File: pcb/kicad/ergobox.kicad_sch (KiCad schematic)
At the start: 72 parts, among them SW1 SW_Push, SW10 Kailh, SW11 Kailh, SW12 Kailh, SW13 Kailh, SW14 Kailh, SW15 Kailh, SW16 Kailh, SW17 Kailh, SW18 Kailh, SW19 Kailh, SW2 SW_Push, SW20 Kailh, SW3 SW_Push, SW4 SW_Push, SW5 SW_Push, SW6 SW_Push, SW7 SW_Push, SW8 SW_Push, SW9 Kailh, U1 TLV73333PDBV, U2 RP2040, U3 W25Q128JVS, Y1 Crystal_GND24

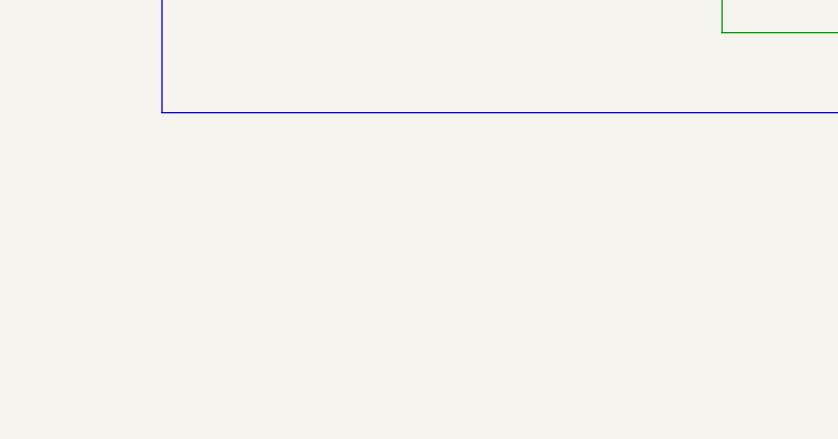
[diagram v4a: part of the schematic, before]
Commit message: feat: adds M4 mounting holes to schematic
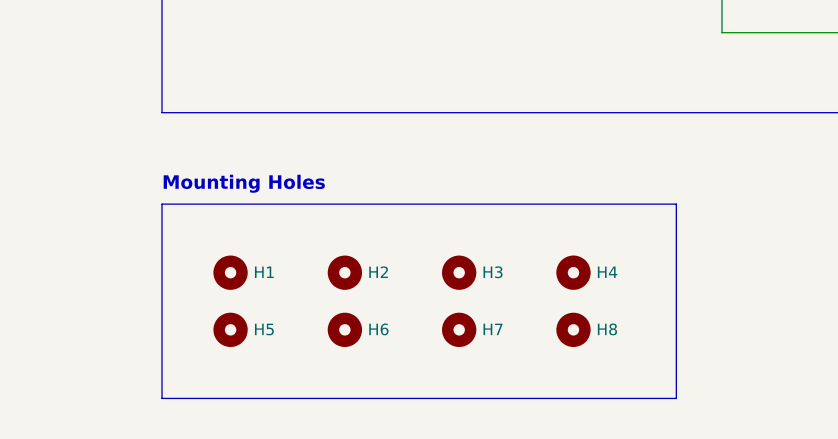
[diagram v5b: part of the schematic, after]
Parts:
- added H1, H2, H3, H4, H5, H6, H7, H8: MountingHole, MountingHole:MountingHole_4.3mm_M4, symbol Mechanical:MountingHole
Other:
- note added: "Mounting Holes"
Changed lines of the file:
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@@
     (stroke (width 0) (type default) (color 0 0 0 0))
   )
+  (polyline (pts (xy 260.35 280.67) (xy 203.2 280.67))
+    (stroke (width 0) (type default) (color 0 0 0 0))
+  )
   (wire (pts (xy 36.83 81.28) (xy 53.34 81.28))
     (stroke (width 0) (type default) (color 0 0 0 0))
@@
     (stroke (width 0) (type default) (color 0 0 0 0))
   )
+  (polyline (pts (xy 203.2 259.08) (xy 260.35 259.08))
+    (stroke (width 0) (type default) (color 0 0 0 0))
+  )
   (wire (pts (xy 111.76 40.64) (xy 111.76 44.45))
     (stroke (width 0) (type default) (color 0 0 0 0))
@@
     (stroke (width 0) (type default) (color 0 0 0 0))
   )
+  (polyline (pts (xy 203.2 259.08) (xy 203.2 280.67))
+    (stroke (width 0) (type default) (color 0 0 0 0))
+  )
   (wire (pts (xy 64.77 46.99) (xy 64.77 55.88))
     (stroke (width 0) (type default) (color 0 0 0 0))
@@
     (stroke (width 0) (type default) (color 0 0 0 0))
   )
+  (polyline (pts (xy 260.35 259.08) (xy 260.35 280.67))
+    (stroke (width 0) (type default) (color 0 0 0 0))
+  )
   (wire (pts (xy 44.45 204.47) (xy 71.12 204.47))
     (stroke (width 0) (type default) (color 0 0 0 0))
@@
     (effects (font (size 1.5 1.5) bold) (justify left bottom))
   )
+  (text "Mounting Holes\n" (at 203.2 257.81 0)
+    (effects (font (size 1.5 1.5) bold) (justify left bottom))
+  )
   (text "Switches" (at 203.2 19.05 0)
     (effects (font (size 1.5 1.5) bold) (justify left bottom))
@@
     (pin "2")
   )
+  (symbol (lib_id "Mechanical:MountingHole") (at 236.22 273.05 0) (unit 1)
+    (in_bom yes) (on_board yes) (fields_autoplaced)
+    (property "Reference" "H7" (id 0) (at 238.76 273.0499 0)
+      (effects (font (size 1.27 1.27)) (justify left))
+    )
+    (property "Value" "MountingHole" (id 1) (at 238.76 274.3199 0)
+      (effects (font (size 1.27 1.27)) (justify left) hide)
+    )
+    (property "Footprint" "MountingHole:MountingHole_4.3mm_M4" (id 2) (at 236.22 273.05 0)
+      (effects (font (size 1.27 1.27)) hide)
+    )
+    (property "Datasheet" "~" (id 3) (at 236.22 273.05 0)
+      (effects (font (size 1.27 1.27)) hide)
+    )
+  )
   (symbol (lib_id "Switch:SW_Push") (at 43.18 127 0) (unit 1)
     (in_bom yes) (on_board yes) (fields_autoplaced)
@@
     (pin "1")
   )
+  (symbol (lib_id "Mechanical:MountingHole") (at 248.92 273.05 0) (unit 1)
+    (in_bom yes) (on_board yes) (fields_autoplaced)
+    (property "Reference" "H8" (id 0) (at 251.46 273.0499 0)
+      (effects (font (size 1.27 1.27)) (justify left))
+    )
+    (property "Value" "MountingHole" (id 1) (at 251.46 274.3199 0)
+      (effects (font (size 1.27 1.27)) (justify left) hide)
+    )
+    (property "Footprint" "MountingHole:MountingHole_4.3mm_M4" (id 2) (at 248.92 273.05 0)
+      (effects (font (size 1.27 1.27)) hide)
+    )
+    (property "Datasheet" "~" (id 3) (at 248.92 273.05 0)
+      (effects (font (size 1.27 1.27)) hide)
+    )
+  )
   (symbol (lib_id "Device:C") (at 69.85 264.16 0) (unit 1)
     (in_bom yes) (on_board yes) (fields_autoplaced)
@@
     (pin "2")
   )
+  (symbol (lib_id "Mechanical:MountingHole") (at 223.52 273.05 0) (unit 1)
+    (in_bom yes) (on_board yes) (fields_autoplaced)
+    (property "Reference" "H6" (id 0) (at 226.06 273.0499 0)
+      (effects (font (size 1.27 1.27)) (justify left))
+    )
+    (property "Value" "MountingHole" (id 1) (at 226.06 274.3199 0)
+      (effects (font (size 1.27 1.27)) (justify left) hide)
+    )
+    (property "Footprint" "MountingHole:MountingHole_4.3mm_M4" (id 2) (at 223.52 273.05 0)
+      (effects (font (size 1.27 1.27)) hide)
+    )
+    (property "Datasheet" "~" (id 3) (at 223.52 273.05 0)
+      (effects (font (size 1.27 1.27)) hide)
+    )
+  )
   (symbol (lib_id "USB-C:HRO-TYPE-C-31-M-12") (at 41.91 205.74 0) (unit 1)
     (in_bom yes) (on_board yes)
@@
     (pin "2")
   )
+  (symbol (lib_id "Mechanical:MountingHole") (at 210.82 266.7 0) (unit 1)
+    (in_bom yes) (on_board yes) (fields_autoplaced)
+    (property "Reference" "H1" (id 0) (at 213.36 266.6999 0)
+      (effects (font (size 1.27 1.27)) (justify left))
+    )
+    (property "Value" "MountingHole" (id 1) (at 213.36 267.9699 0)
+      (effects (font (size 1.27 1.27)) (justify left) hide)
+    )
+    (property "Footprint" "MountingHole:MountingHole_4.3mm_M4" (id 2) (at 210.82 266.7 0)
+      (effects (font (size 1.27 1.27)) hide)
+    )
+    (property "Datasheet" "~" (id 3) (at 210.82 266.7 0)
+      (effects (font (size 1.27 1.27)) hide)
+    )
+  )
   (symbol (lib_id "power:GND") (at 69.85 270.51 0) (unit 1)
     (in_bom yes) (on_board yes) (fields_autoplaced)
@@
     (pin "1")
   )
+  (symbol (lib_id "Mechanical:MountingHole") (at 223.52 266.7 0) (unit 1)
+    (in_bom yes) (on_board yes) (fields_autoplaced)
+    (property "Reference" "H2" (id 0) (at 226.06 266.6999 0)
+      (effects (font (size 1.27 1.27)) (justify left))
+    )
+    (property "Value" "MountingHole" (id 1) (at 226.06 267.9699 0)
+      (effects (font (size 1.27 1.27)) (justify left) hide)
+    )
+    (property "Footprint" "MountingHole:MountingHole_4.3mm_M4" (id 2) (at 223.52 266.7 0)
+      (effects (font (size 1.27 1.27)) hide)
+    )
+    (property "Datasheet" "~" (id 3) (at 223.52 266.7 0)
+      (effects (font (size 1.27 1.27)) hide)
+    )
+  )
   (symbol (lib_id "Switch:SW_Push") (at 266.7 46.99 0) (unit 1)
     (in_bom yes) (on_board yes) (fields_autoplaced)
@@
     (pin "4")
   )
+  (symbol (lib_id "Mechanical:MountingHole") (at 210.82 273.05 0) (unit 1)
+    (in_bom yes) (on_board yes) (fields_autoplaced)
+    (property "Reference" "H5" (id 0) (at 213.36 273.0499 0)
+      (effects (font (size 1.27 1.27)) (justify left))
+    )
+    (property "Value" "MountingHole" (id 1) (at 213.36 274.3199 0)
+      (effects (font (size 1.27 1.27)) (justify left) hide)
+    )
+    (property "Footprint" "MountingHole:MountingHole_4.3mm_M4" (id 2) (at 210.82 273.05 0)
+      (effects (font (size 1.27 1.27)) hide)
+    )
+    (property "Datasheet" "~" (id 3) (at 210.82 273.05 0)
+      (effects (font (size 1.27 1.27)) hide)
+    )
+  )
   (symbol (lib_id "Device:C") (at 256.54 195.58 0) (unit 1)
     (in_bom yes) (on_board yes)
@@
     (pin "1")
   )
+  (symbol (lib_id "Mechanical:MountingHole") (at 236.22 266.7 0) (unit 1)
+    (in_bom yes) (on_board yes) (fields_autoplaced)
+    (property "Reference" "H3" (id 0) (at 238.76 266.6999 0)
+      (effects (font (size 1.27 1.27)) (justify left))
+    )
+    (property "Value" "MountingHole" (id 1) (at 238.76 267.9699 0)
+      (effects (font (size 1.27 1.27)) (justify left) hide)
+    )
+    (property "Footprint" "MountingHole:MountingHole_4.3mm_M4" (id 2) (at 236.22 266.7 0)
+      (effects (font (size 1.27 1.27)) hide)
+    )
+    (property "Datasheet" "~" (id 3) (at 236.22 266.7 0)
+      (effects (font (size 1.27 1.27)) hide)
+    )
+  )
   (symbol (lib_id "Device:C") (at 167.64 36.83 0) (unit 1)
     (in_bom yes) (on_board yes) (fields_autoplaced)
@@
     (pin "2")
   )
+  (symbol (lib_id "Mechanical:MountingHole") (at 248.92 266.7 0) (unit 1)
+    (in_bom yes) (on_board yes) (fields_autoplaced)
+    (property "Reference" "H4" (id 0) (at 251.46 266.6999 0)
+      (effects (font (size 1.27 1.27)) (justify left))
+    )
+    (property "Value" "MountingHole" (id 1) (at 251.46 267.9699 0)
+      (effects (font (size 1.27 1.27)) (justify left) hide)
+    )
+    (property "Footprint" "MountingHole:MountingHole_4.3mm_M4" (id 2) (at 248.92 266.7 0)
+      (effects (font (size 1.27 1.27)) hide)
+    )
+    (property "Datasheet" "~" (id 3) (at 248.92 266.7 0)
+      (effects (font (size 1.27 1.27)) hide)
+    )
+  )
   (symbol (lib_id "Switch:SW_Push") (at 110.49 269.24 90) (unit 1)
     (in_bom yes) (on_board yes)
@@
       (reference "D12") (unit 1) (value "WS2812C-2020") (footprint "WS2812C-2020:LED_WS2812C-2020")
     )
+    (path "/687e50ab-3031-4d58-8b19-d1b9b19cede1"
+      (reference "H1") (unit 1) (value "MountingHole") (footprint "MountingHole:MountingHole_4.3mm_M4")
+    )
+    (path "/6c8cfcb3-2d0d-4436-a20a-c00cae63ff2f"
+      (reference "H2") (unit 1) (value "MountingHole") (footprint "MountingHole:MountingHole_4.3mm_M4")
+    )
+    (path "/8a16ad91-6558-4e06-9814-73d3ba261d92"
+      (reference "H3") (unit 1) (value "MountingHole") (footprint "MountingHole:MountingHole_4.3mm_M4")
+    )
+    (path "/da7f181c-d15d-4405-8b7c-eeb7f5b635a9"
+      (reference "H4") (unit 1) (value "MountingHole") (footprint "MountingHole:MountingHole_4.3mm_M4")
+    )
+    (path "/80f2d6a0-2d04-463b-980a-3c1edca108b9"
+      (reference "H5") (unit 1) (value "MountingHole") (footprint "MountingHole:MountingHole_4.3mm_M4")
+    )
+    (path "/3f875e20-671c-43b5-8a63-545e16b7fd63"
+      (reference "H6") (unit 1) (value "MountingHole") (footprint "MountingHole:MountingHole_4.3mm_M4")
+    )
+    (path "/2bc49a6e-0559-4615-be88-bf9131f58e2b"
+      (reference "H7") (unit 1) (value "MountingHole") (footprint "MountingHole:MountingHole_4.3mm_M4")
+    )
+    (path "/3435fb98-ae2e-4861-b6f5-7fd7a7ca1bfc"
+      (reference "H8") (unit 1) (value "MountingHole") (footprint "MountingHole:MountingHole_4.3mm_M4")
+    )
     (path "/f641fac0-9443-4e6d-9146-0822ee3cea7e"

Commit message: feat: initial PCB setup
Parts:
- H5: footprint MountingHole:MountingHole_4.3mm_M4 -> MountingHole:MountingHole_3.2mm_M3
- U2: footprint RP2040_minimal:RP2040-QFN-56 -> RP2040:RP2040-QFN-56
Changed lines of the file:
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@@
       (effects (font (size 1.27 1.27)) (justify left) hide)
     )
-    (property "Footprint" "MountingHole:MountingHole_4.3mm_M4" (id 2) (at 210.82 273.05 0)
+    (property "Footprint" "MountingHole:MountingHole_3.2mm_M3" (id 2) (at 210.82 273.05 0)
       (effects (font (size 1.27 1.27)) hide)
     )
@@
       (effects (font (size 1.27 1.27)) (justify left))
     )
-    (property "Footprint" "RP2040_minimal:RP2040-QFN-56" (id 2) (at 66.04 106.68 0)
+    (property "Footprint" "RP2040:RP2040-QFN-56" (id 2) (at 66.04 106.68 0)
       (effects (font (size 1.27 1.27)) hide)
     )
@@
     )
     (path "/80f2d6a0-2d04-463b-980a-3c1edca108b9"
-      (reference "H5") (unit 1) (value "MountingHole") (footprint "MountingHole:MountingHole_4.3mm_M4")
+      (reference "H5") (unit 1) (value "MountingHole") (footprint "MountingHole:MountingHole_3.2mm_M3")
     )
     (path "/3f875e20-671c-43b5-8a63-545e16b7fd63"
@@
     )
     (path "/9ba26deb-2dd5-446d-bf34-3cafd3f511c3"
-      (reference "U2") (unit 1) (value "RP2040") (footprint "RP2040_minimal:RP2040-QFN-56")
+      (reference "U2") (unit 1) (value "RP2040") (footprint "RP2040:RP2040-QFN-56")
     )
     (path "/91d5d34b-e030-491a-8afc-6eb190fc6b2f"

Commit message: refactor: changes kailh footprints to hotswap non-optionals.
The kailh low footprints with optional hotswaps are not symmetric.
In the optional footprint, the hotswap switch pad goes through the RGB footpad,
so it cannot be used.
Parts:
- SW10, SW11, SW12, SW13, SW14, SW15, SW16, SW17, SW18, SW19, SW20, SW9: footprint Keyswitches:Kailh_socket_PG1350_optional -> Keyswitches:Kailh_socket_PG1350
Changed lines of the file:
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@@
     (property "Reference" "SW11" (id 0) (at 266.7 50.8 0))
     (property "Value" "Kailh" (id 1) (at 266.7 53.34 0))
-    (property "Footprint" "Keyswitches:Kailh_socket_PG1350_optional" (id 2) (at 266.7 53.34 0)
+    (property "Footprint" "Keyswitches:Kailh_socket_PG1350" (id 2) (at 266.7 53.34 0)
       (effects (font (size 1.27 1.27)) hide)
     )
@@
     (property "Reference" "SW17" (id 0) (at 344.17 27.94 0))
     (property "Value" "Kailh" (id 1) (at 344.17 30.48 0))
-    (property "Footprint" "Keyswitches:Kailh_socket_PG1350_optional" (id 2) (at 344.17 30.48 0)
+    (property "Footprint" "Keyswitches:Kailh_socket_PG1350" (id 2) (at 344.17 30.48 0)
       (effects (font (size 1.27 1.27)) hide)
     )
@@
     (property "Reference" "SW16" (id 0) (at 304.8 62.23 0))
     (property "Value" "Kailh" (id 1) (at 304.8 64.77 0))
-    (property "Footprint" "Keyswitches:Kailh_socket_PG1350_optional" (id 2) (at 304.8 64.77 0)
+    (property "Footprint" "Keyswitches:Kailh_socket_PG1350" (id 2) (at 304.8 64.77 0)
       (effects (font (size 1.27 1.27)) hide)
     )
@@
     (property "Reference" "SW12" (id 0) (at 266.7 62.23 0))
     (property "Value" "Kailh" (id 1) (at 266.7 64.77 0))
-    (property "Footprint" "Keyswitches:Kailh_socket_PG1350_optional" (id 2) (at 266.7 64.77 0)
+    (property "Footprint" "Keyswitches:Kailh_socket_PG1350" (id 2) (at 266.7 64.77 0)
       (effects (font (size 1.27 1.27)) hide)
     )
@@
     (property "Reference" "SW14" (id 0) (at 304.8 39.37 0))
     (property "Value" "Kailh" (id 1) (at 304.8 41.91 0))
-    (property "Footprint" "Keyswitches:Kailh_socket_PG1350_optional" (id 2) (at 304.8 41.91 0)
+    (property "Footprint" "Keyswitches:Kailh_socket_PG1350" (id 2) (at 304.8 41.91 0)
       (effects (font (size 1.27 1.27)) hide)
     )
@@
     (property "Reference" "SW20" (id 0) (at 344.17 62.23 0))
     (property "Value" "Kailh" (id 1) (at 344.17 64.77 0))
-    (property "Footprint" "Keyswitches:Kailh_socket_PG1350_optional" (id 2) (at 344.17 64.77 0)
+    (property "Footprint" "Keyswitches:Kailh_socket_PG1350" (id 2) (at 344.17 64.77 0)
       (effects (font (size 1.27 1.27)) hide)
     )
@@
     (property "Reference" "SW10" (id 0) (at 266.7 39.37 0))
     (property "Value" "Kailh" (id 1) (at 266.7 41.91 0))
-    (property "Footprint" "Keyswitches:Kailh_socket_PG1350_optional" (id 2) (at 266.7 41.91 0)
+    (property "Footprint" "Keyswitches:Kailh_socket_PG1350" (id 2) (at 266.7 41.91 0)
       (effects (font (size 1.27 1.27)) hide)
     )
@@
     (property "Reference" "SW19" (id 0) (at 344.17 50.8 0))
     (property "Value" "Kailh" (id 1) (at 344.17 53.34 0))
-    (property "Footprint" "Keyswitches:Kailh_socket_PG1350_optional" (id 2) (at 344.17 53.34 0)
+    (property "Footprint" "Keyswitches:Kailh_socket_PG1350" (id 2) (at 344.17 53.34 0)
       (effects (font (size 1.27 1.27)) hide)
     )
@@
     (property "Reference" "SW18" (id 0) (at 344.17 39.37 0))
     (property "Value" "Kailh" (id 1) (at 344.17 41.91 0))
-    (property "Footprint" "Keyswitches:Kailh_socket_PG1350_optional" (id 2) (at 344.17 41.91 0)
+    (property "Footprint" "Keyswitches:Kailh_socket_PG1350" (id 2) (at 344.17 41.91 0)
       (effects (font (size 1.27 1.27)) hide)
     )
@@
     (property "Reference" "SW15" (id 0) (at 304.8 50.8 0))
     (property "Value" "Kailh" (id 1) (at 304.8 53.34 0))
-    (property "Footprint" "Keyswitches:Kailh_socket_PG1350_optional" (id 2) (at 304.8 53.34 0)
+    (property "Footprint" "Keyswitches:Kailh_socket_PG1350" (id 2) (at 304.8 53.34 0)
       (effects (font (size 1.27 1.27)) hide)
     )
@@
     (property "Reference" "SW9" (id 0) (at 266.7 27.94 0))
     (property "Value" "Kailh" (id 1) (at 266.7 30.48 0))
-    (property "Footprint" "Keyswitches:Kailh_socket_PG1350_optional" (id 2) (at 266.7 30.48 0)
+    (property "Footprint" "Keyswitches:Kailh_socket_PG1350" (id 2) (at 266.7 30.48 0)
       (effects (font (size 1.27 1.27)) hide)
     )
@@
     (property "Reference" "SW13" (id 0) (at 304.8 27.94 0))
     (property "Value" "Kailh" (id 1) (at 304.8 30.48 0))
-    (property "Footprint" "Keyswitches:Kailh_socket_PG1350_optional" (id 2) (at 304.8 30.48 0)
+    (property "Footprint" "Keyswitches:Kailh_socket_PG1350" (id 2) (at 304.8 30.48 0)
       (effects (font (size 1.27 1.27)) hide)
     )
@@
     )
     (path "/e7e50001-1420-4b1c-9a9c-244be6cee891"
-      (reference "SW9") (unit 1) (value "Kailh") (footprint "Keyswitches:Kailh_socket_PG1350_optional")
+      (reference "SW9") (unit 1) (value "Kailh") (footprint "Keyswitches:Kailh_socket_PG1350")
     )
     (path "/6ffa2bda-adb8-4b45-b2f3-66d14af70739"
-      (reference "SW10") (unit 1) (value "Kailh") (footprint "Keyswitches:Kailh_socket_PG1350_optional")
+      (reference "SW10") (unit 1) (value "Kailh") (footprint "Keyswitches:Kailh_socket_PG1350")
     )
     (path "/0d5161b8-5c58-4924-99b4-8ca9b7edfc0a"
-      (reference "SW11") (unit 1) (value "Kailh") (footprint "Keyswitches:Kailh_socket_PG1350_optional")
+      (reference "SW11") (unit 1) (value "Kailh") (footprint "Keyswitches:Kailh_socket_PG1350")
     )
     (path "/4a2c44e2-5354-4d12-93e7-55de66eaf6db"
-      (reference "SW12") (unit 1) (value "Kailh") (footprint "Keyswitches:Kailh_socket_PG1350_optional")
+      (reference "SW12") (unit 1) (value "Kailh") (footprint "Keyswitches:Kailh_socket_PG1350")
     )
     (path "/f782518d-1e58-45b8-86df-64b2f301f57b"
-      (reference "SW13") (unit 1) (value "Kailh") (footprint "Keyswitches:Kailh_socket_PG1350_optional")
+      (reference "SW13") (unit 1) (value "Kailh") (footprint "Keyswitches:Kailh_socket_PG1350")
     )
     (path "/53fbce93-16c6-4ed7-9a04-6a5f272cab51"
-      (reference "SW14") (unit 1) (value "Kailh") (footprint "Keyswitches:Kailh_socket_PG1350_optional")
+      (reference "SW14") (unit 1) (value "Kailh") (footprint "Keyswitches:Kailh_socket_PG1350")
     )
     (path "/d72db84b-8b36-4381-8bae-7e7b8e71a550"
-      (reference "SW15") (unit 1) (value "Kailh") (footprint "Keyswitches:Kailh_socket_PG1350_optional")
+      (reference "SW15") (unit 1) (value "Kailh") (footprint "Keyswitches:Kailh_socket_PG1350")
     )
     (path "/2d890ef2-4562-41a2-a026-1abb741422ac"
-      (reference "SW16") (unit 1) (value "Kailh") (footprint "Keyswitches:Kailh_socket_PG1350_optional")
+      (reference "SW16") (unit 1) (value "Kailh") (footprint "Keyswitches:Kailh_socket_PG1350")
     )
     (path "/19b0ce15-4c08-412b-87c9-e357c06d1577"
-      (reference "SW17") (unit 1) (value "Kailh") (footprint "Keyswitches:Kailh_socket_PG1350_optional")
+      (reference "SW17") (unit 1) (value "Kailh") (footprint "Keyswitches:Kailh_socket_PG1350")
     )
     (path "/bf14133a-e3dd-4876-94ab-bfabcac675ee"
-      (reference "SW18") (unit 1) (value "Kailh") (footprint "Keyswitches:Kailh_socket_PG1350_optional")
+      (reference "SW18") (unit 1) (value "Kailh") (footprint "Keyswitches:Kailh_socket_PG1350")
     )
     (path "/b30149f7-7340-4a08-a501-4fd458ccf120"
-      (reference "SW19") (unit 1) (value "Kailh") (footprint "Keyswitches:Kailh_socket_PG1350_optional")
+      (reference "SW19") (unit 1) (value "Kailh") (footprint "Keyswitches:Kailh_socket_PG1350")
     )
     (path "/677ff06d-f79f-4636-ba21-beec29f993c2"
-      (reference "SW20") (unit 1) (value "Kailh") (footprint "Keyswitches:Kailh_socket_PG1350_optional")
+      (reference "SW20") (unit 1) (value "Kailh") (footprint "Keyswitches:Kailh_socket_PG1350")
     )
     (path "/fe9c4ac9-a70d-46e0-af36-a86bcd3800dd"

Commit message: feat: introduces GND plane on B.Cu
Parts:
- H5: footprint MountingHole:MountingHole_3.2mm_M3 -> MountingHole:MountingHole_4.3mm_M4
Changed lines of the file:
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@@
       (effects (font (size 1.27 1.27)) (justify left) hide)
     )
-    (property "Footprint" "MountingHole:MountingHole_3.2mm_M3" (id 2) (at 210.82 273.05 0)
+    (property "Footprint" "MountingHole:MountingHole_4.3mm_M4" (id 2) (at 210.82 273.05 0)
       (effects (font (size 1.27 1.27)) hide)
     )
@@
     )
     (path "/80f2d6a0-2d04-463b-980a-3c1edca108b9"
-      (reference "H5") (unit 1) (value "MountingHole") (footprint "MountingHole:MountingHole_3.2mm_M3")
+      (reference "H5") (unit 1) (value "MountingHole") (footprint "MountingHole:MountingHole_4.3mm_M4")
     )
     (path "/3f875e20-671c-43b5-8a63-545e16b7fd63"
